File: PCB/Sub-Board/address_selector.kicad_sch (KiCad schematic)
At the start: 10 parts, among them SW1 SW_DIP_x07

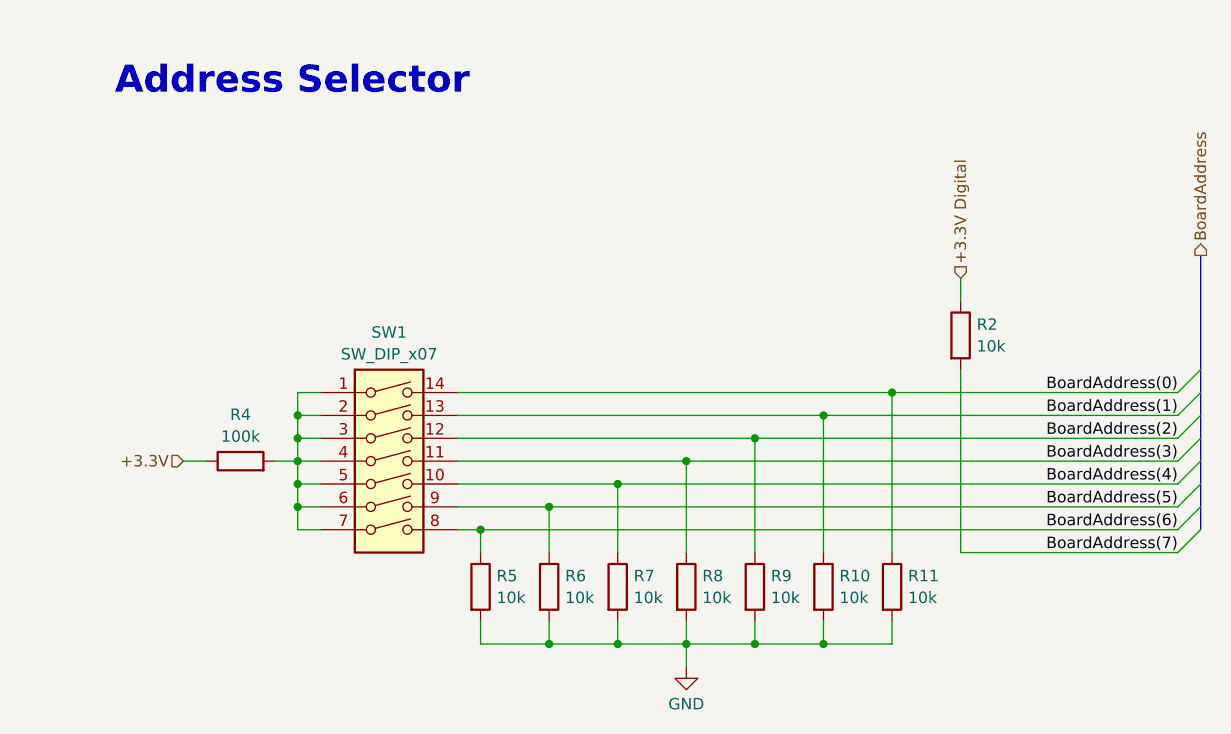
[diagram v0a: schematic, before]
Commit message: Sub-Board PCB before ERC
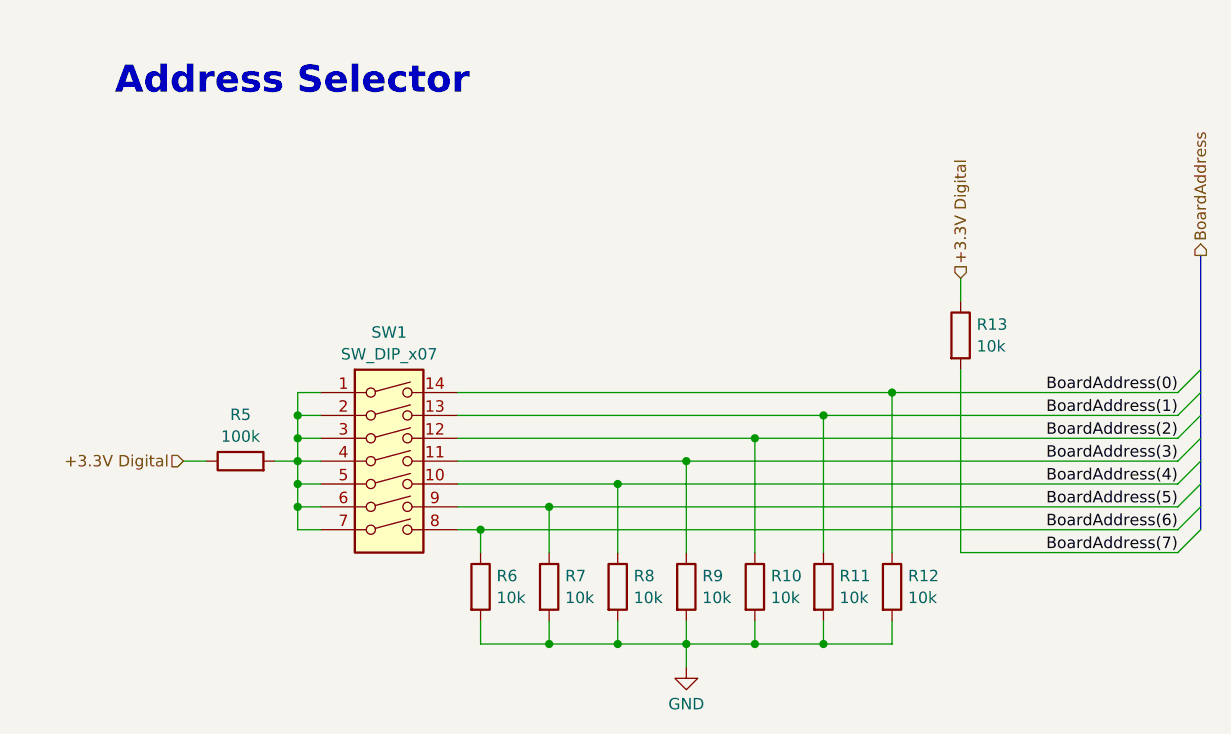
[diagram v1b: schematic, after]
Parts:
- renumbered R9 to R10, R10 to R11, R11 to R12, R2 to R13, R4 to R5, R5 to R6, R6 to R7, R7 to R8, R8 to R9
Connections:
- net +3.3V is gone; now on net +3.3V Digital: R5.1
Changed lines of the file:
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@@
 		)
 	)
-	(hierarchical_label "+3.3V"
+	(hierarchical_label "+3.3V Digital"
 		(shape input)
 		(at 33.02 69.85 180)
@@
 		(dnp no)
 		(fields_autoplaced yes)
-		(property "Reference" "R8"
+		(property "Reference" "R9"
 			(at 90.678 82.6078 0)
 			(effects
@@
 			(project "Template"
 				(path "/f9cf8dcb-b299-4fad-bb24-e1dfd3a00b1a/0d3a9f9f-f57a-40a2-884d-240f1a33dfd6"
-					(reference "R8")
+					(reference "R9")
 					(unit 1)
 				)
@@
 		(dnp no)
 		(fields_autoplaced yes)
-		(property "Reference" "R11"
+		(property "Reference" "R12"
 			(at 113.538 82.6078 0)
 			(effects
@@
 			(project "Template"
 				(path "/f9cf8dcb-b299-4fad-bb24-e1dfd3a00b1a/0d3a9f9f-f57a-40a2-884d-240f1a33dfd6"
-					(reference "R11")
+					(reference "R12")
 					(unit 1)
 				)
@@
 		(dnp no)
 		(fields_autoplaced yes)
-		(property "Reference" "R7"
+		(property "Reference" "R8"
 			(at 83.058 82.6078 0)
 			(effects
@@
 			(project "Template"
 				(path "/f9cf8dcb-b299-4fad-bb24-e1dfd3a00b1a/0d3a9f9f-f57a-40a2-884d-240f1a33dfd6"
-					(reference "R7")
+					(reference "R8")
 					(unit 1)
 				)
@@
 		(dnp no)
 		(fields_autoplaced yes)
-		(property "Reference" "R2"
+		(property "Reference" "R13"
 			(at 121.158 54.6678 0)
 			(effects
@@
 			(project "Template"
 				(path "/f9cf8dcb-b299-4fad-bb24-e1dfd3a00b1a/0d3a9f9f-f57a-40a2-884d-240f1a33dfd6"
-					(reference "R2")
+					(reference "R13")
 					(unit 1)
 				)
@@
 		(dnp no)
 		(fields_autoplaced yes)
-		(property "Reference" "R9"
+		(property "Reference" "R10"
 			(at 98.298 82.6078 0)
 			(effects
@@
 			(project "Template"
 				(path "/f9cf8dcb-b299-4fad-bb24-e1dfd3a00b1a/0d3a9f9f-f57a-40a2-884d-240f1a33dfd6"
-					(reference "R9")
+					(reference "R10")
 					(unit 1)
 				)
@@
 		(dnp no)
 		(fields_autoplaced yes)
-		(property "Reference" "R5"
+		(property "Reference" "R6"
 			(at 67.818 82.6078 0)
 			(effects
@@
 			(project "Template"
 				(path "/f9cf8dcb-b299-4fad-bb24-e1dfd3a00b1a/0d3a9f9f-f57a-40a2-884d-240f1a33dfd6"
-					(reference "R5")
+					(reference "R6")
 					(unit 1)
 				)
@@
 		(dnp no)
 		(fields_autoplaced yes)
-		(property "Reference" "R4"
+		(property "Reference" "R5"
 			(at 39.37 64.6895 90)
 			(effects
@@
 			(project "Template"
 				(path "/f9cf8dcb-b299-4fad-bb24-e1dfd3a00b1a/0d3a9f9f-f57a-40a2-884d-240f1a33dfd6"
-					(reference "R4")
+					(reference "R5")
 					(unit 1)
 				)
@@
 		(dnp no)
 		(fields_autoplaced yes)
-		(property "Reference" "R10"
+		(property "Reference" "R11"
 			(at 105.918 82.6078 0)
 			(effects
@@
 			(project "Template"
 				(path "/f9cf8dcb-b299-4fad-bb24-e1dfd3a00b1a/0d3a9f9f-f57a-40a2-884d-240f1a33dfd6"
-					(reference "R10")
+					(reference "R11")
 					(unit 1)
 				)
@@
 		(dnp no)
 		(fields_autoplaced yes)
-		(property "Reference" "R6"
+		(property "Reference" "R7"
 			(at 75.438 82.6078 0)
 			(effects
@@
 			(project "Template"
 				(path "/f9cf8dcb-b299-4fad-bb24-e1dfd3a00b1a/0d3a9f9f-f57a-40a2-884d-240f1a33dfd6"
-					(reference "R6")
-					(unit 1)
-				)
+					(reference "R7")
+					(unit 1)
+				)

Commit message: Sub-Board PCB after ERC
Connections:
- net BoardAddress(0) renamed BoardAddress0
- net BoardAddress(1) renamed BoardAddress1
- net BoardAddress(2) renamed BoardAddress2
- net BoardAddress(3) renamed BoardAddress3
- net BoardAddress(4) renamed BoardAddress4
- net BoardAddress(5) renamed BoardAddress5
- net BoardAddress(6) renamed BoardAddress6
- net BoardAddress(7) renamed BoardAddress7
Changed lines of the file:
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@@
 		)
 	)
-	(label "BoardAddress(2)"
+	(label "BoardAddress2"
 		(at 143.51 67.31 180)
 		(effects
@@
 		)
 	)
-	(label "BoardAddress(3)"
+	(label "BoardAddress3"
 		(at 143.51 69.85 180)
 		(effects
@@
 		)
 	)
-	(label "BoardAddress(0)"
+	(label "BoardAddress0"
 		(at 143.51 62.23 180)
 		(effects
@@
 		)
 	)
-	(label "BoardAddress(1)"
+	(label "BoardAddress1"
 		(at 143.51 64.77 180)
 		(effects
@@
 		)
 	)
-	(label "BoardAddress(7)"
+	(label "BoardAddress7"
 		(at 143.51 80.01 180)
 		(effects
@@
 		)
 	)
-	(label "BoardAddress(4)"
+	(label "BoardAddress4"
 		(at 143.51 72.39 180)
 		(effects
@@
 		)
 	)
-	(label "BoardAddress(5)"
+	(label "BoardAddress5"
 		(at 143.51 74.93 180)
 		(effects
@@
 		)
 	)
-	(label "BoardAddress(6)"
+	(label "BoardAddress6"
 		(at 143.51 77.47 180)
 		(effects
@@
 		)
 	)
-	(hierarchical_label "BoardAddress"
+	(hierarchical_label "BoardAddress[0..7]"
 		(shape output)
 		(at 146.05 46.99 90)

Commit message: Sub-Board PCB: Footprint assignments
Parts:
- R10, R11, R12, R13, R5, R6, R7, R8, R9: footprint (none) -> Resistor_SMD:R_0603_1608Metric
- SW1: footprint (none) -> Button_Switch_SMD:SW_DIP_SPSTx07_Slide_6.7x19.34mm_W6.73mm_P2.54mm_LowProfile_JPin
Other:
- title: Modular Music Controller – Address Selector -> Modular Music Controller / Sub-Board / Address Selector
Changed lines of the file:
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@@
 	(paper "A4")
 	(title_block
-		(title "Modular Music Controller – Address Selector")
+		(title "Modular Music Controller / Sub-Board / Address Selector")
 		(date "2025-11-02")
 		(rev "1")
@@
 			)
 		)
-		(property "Footprint" ""
+		(property "Footprint" "Resistor_SMD:R_0603_1608Metric"
 			(at 87.122 83.82 90)
 			(effects
@@
 			)
 		)
-		(property "Footprint" ""
+		(property "Footprint" "Resistor_SMD:R_0603_1608Metric"
 			(at 109.982 83.82 90)
 			(effects
@@
 			)
 		)
-		(property "Footprint" ""
+		(property "Footprint" "Button_Switch_SMD:SW_DIP_SPSTx07_Slide_6.7x19.34mm_W6.73mm_P2.54mm_LowProfile_JPin"
 			(at 55.88 72.39 0)
 			(effects
@@
 			)
 		)
-		(property "Footprint" ""
+		(property "Footprint" "Resistor_SMD:R_0603_1608Metric"
 			(at 79.502 83.82 90)
 			(effects
@@
 			)
 		)
-		(property "Footprint" ""
+		(property "Footprint" "Resistor_SMD:R_0603_1608Metric"
 			(at 117.602 55.88 90)
 			(effects
@@
 			)
 		)
-		(property "Footprint" ""
+		(property "Footprint" "Resistor_SMD:R_0603_1608Metric"
 			(at 94.742 83.82 90)
 			(effects
@@
 			)
 		)
-		(property "Footprint" ""
+		(property "Footprint" "Resistor_SMD:R_0603_1608Metric"
 			(at 64.262 83.82 90)
 			(effects
@@
 			)
 		)
-		(property "Footprint" ""
+		(property "Footprint" "Resistor_SMD:R_0603_1608Metric"
 			(at 39.37 71.628 90)
 			(effects
@@
 			)
 		)
-		(property "Footprint" ""
+		(property "Footprint" "Resistor_SMD:R_0603_1608Metric"
 			(at 102.362 83.82 90)
 			(effects
@@
 			)
 		)
-		(property "Footprint" ""
+		(property "Footprint" "Resistor_SMD:R_0603_1608Metric"
 			(at 71.882 83.82 90)
 			(effects

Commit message: Sub Board PCB: PCB Layout (wip)
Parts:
- R10, R11, R12, R13, R5, R6, R7, R8, R9: footprint Resistor_SMD:R_0603_1608Metric -> Resistor_SMD:R_0402_1005Metric
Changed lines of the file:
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@@
 			)
 		)
-		(property "Footprint" "Resistor_SMD:R_0603_1608Metric"
+		(property "Footprint" "Resistor_SMD:R_0402_1005Metric"
 			(at 87.122 83.82 90)
 			(effects
@@
 			)
 		)
-		(property "Footprint" "Resistor_SMD:R_0603_1608Metric"
+		(property "Footprint" "Resistor_SMD:R_0402_1005Metric"
 			(at 109.982 83.82 90)
 			(effects
@@
 			)
 		)
-		(property "Footprint" "Resistor_SMD:R_0603_1608Metric"
+		(property "Footprint" "Resistor_SMD:R_0402_1005Metric"
 			(at 79.502 83.82 90)
 			(effects
@@
 			)
 		)
-		(property "Footprint" "Resistor_SMD:R_0603_1608Metric"
+		(property "Footprint" "Resistor_SMD:R_0402_1005Metric"
 			(at 117.602 55.88 90)
 			(effects
@@
 			)
 		)
-		(property "Footprint" "Resistor_SMD:R_0603_1608Metric"
+		(property "Footprint" "Resistor_SMD:R_0402_1005Metric"
 			(at 94.742 83.82 90)
 			(effects
@@
 			)
 		)
-		(property "Footprint" "Resistor_SMD:R_0603_1608Metric"
+		(property "Footprint" "Resistor_SMD:R_0402_1005Metric"
 			(at 64.262 83.82 90)
 			(effects
@@
 			)
 		)
-		(property "Footprint" "Resistor_SMD:R_0603_1608Metric"
+		(property "Footprint" "Resistor_SMD:R_0402_1005Metric"
 			(at 39.37 71.628 90)
 			(effects
@@
 			)
 		)
-		(property "Footprint" "Resistor_SMD:R_0603_1608Metric"
+		(property "Footprint" "Resistor_SMD:R_0402_1005Metric"
 			(at 102.362 83.82 90)
 			(effects
@@
 			)
 		)
-		(property "Footprint" "Resistor_SMD:R_0603_1608Metric"
+		(property "Footprint" "Resistor_SMD:R_0402_1005Metric"
 			(at 71.882 83.82 90)
 			(effects

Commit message: Sub Board PCB: Parts Placement (wip)
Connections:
- net BoardAddress0: now also R6.1, SW1.8; no longer R12.1, SW1.14
- net BoardAddress1: now also R7.1, SW1.9; no longer R11.1, SW1.13
- net BoardAddress2: now also R8.1, SW1.10; no longer R10.1, SW1.12
- net BoardAddress4: now also R10.1, SW1.12; no longer R8.1, SW1.10
- net BoardAddress5: now also R11.1, SW1.13; no longer R7.1, SW1.9
- net BoardAddress6: now also R12.1, SW1.14; no longer R6.1, SW1.8
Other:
- moved on the sheet: R13

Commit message: Sub Board PCB: GND/GNDD
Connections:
- net GND renamed GNDD
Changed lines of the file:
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@@
 		(dnp no)
 		(fields_autoplaced yes)
-		(property "Reference" "#PWR08"
+		(property "Reference" "#PWR8"
 			(at 88.9 99.06 0)
 			(effects
@@
 			)
 		)
-		(property "Value" "GND"
+		(property "Value" "GNDD"
 			(at 88.9 96.8431 0)
 			(effects
@@
 			(project "Template"
 				(path "/f9cf8dcb-b299-4fad-bb24-e1dfd3a00b1a/0d3a9f9f-f57a-40a2-884d-240f1a33dfd6"
-					(reference "#PWR08")
+					(reference "#PWR8")
 					(unit 1)
 				)
